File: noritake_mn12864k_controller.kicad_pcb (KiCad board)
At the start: 4 copper layers, 120 parts, among them J1 Conn_01x11, J2 USB_C_Receptacle_USB2.0, J3 TagConnect_TC2030_SWD, Q1 AO3400A, Q10 2N7002, Q11 LBSS84LT1G, Q12 2N7002, Q2 AO3400A, Q3 S9015, Q4 AO3401A, Q5 AO3401A, Q6 S9015, Q7 2N7002, Q8 LBSS84LT1G, Q9 2N7002, T1 Wuerth 760390013, T2 Wuerth 760390013, T3 Wuerth 760390013, U1 SN74AVC8T245PW, U10 XL6007E1, U2 74HC14, U3 CD4051B, U4 MN12864K, U5 STM32F730R8T6, U6 NE555D, U7 74HC08, U8 SRV05-4, U9 XC6206PxxxMR

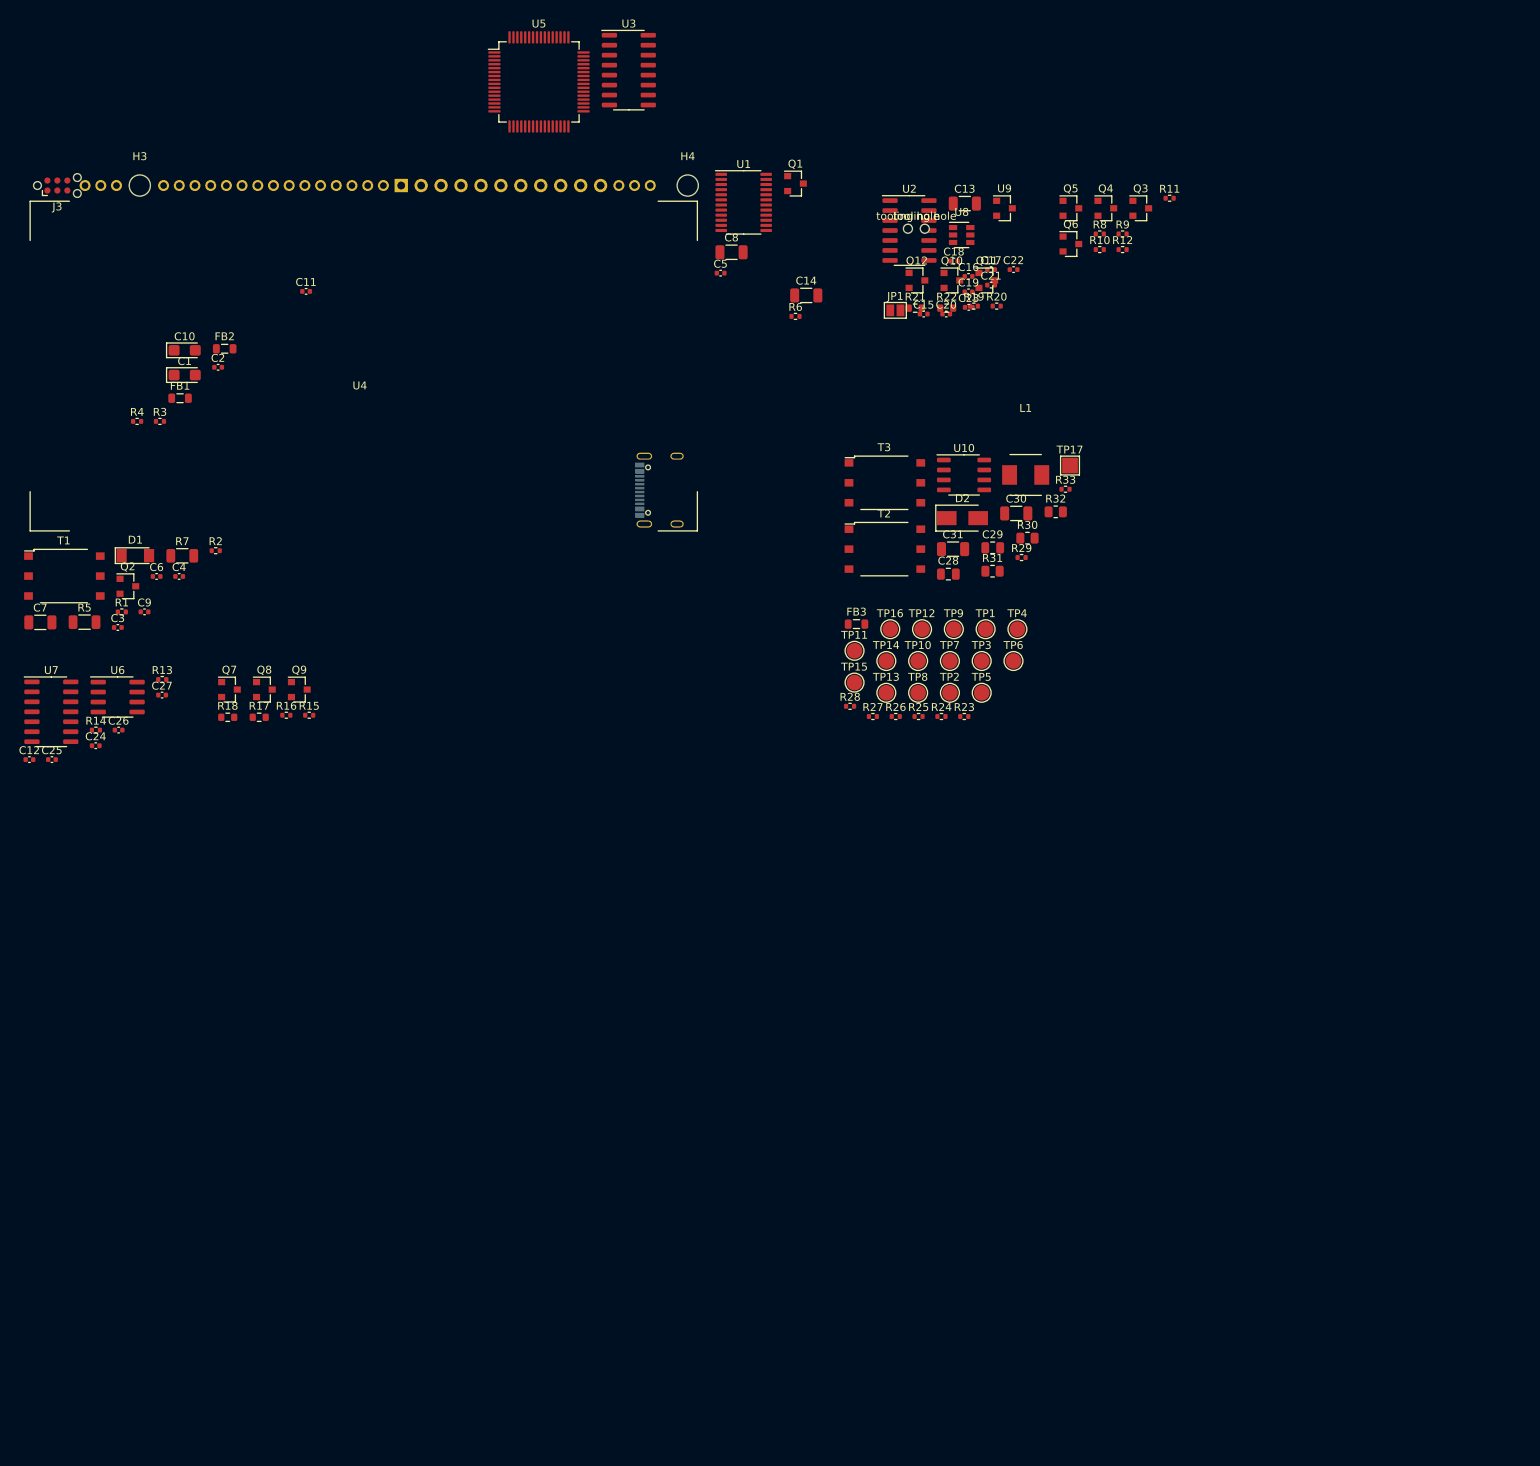
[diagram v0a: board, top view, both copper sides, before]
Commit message: Complete intra section layout
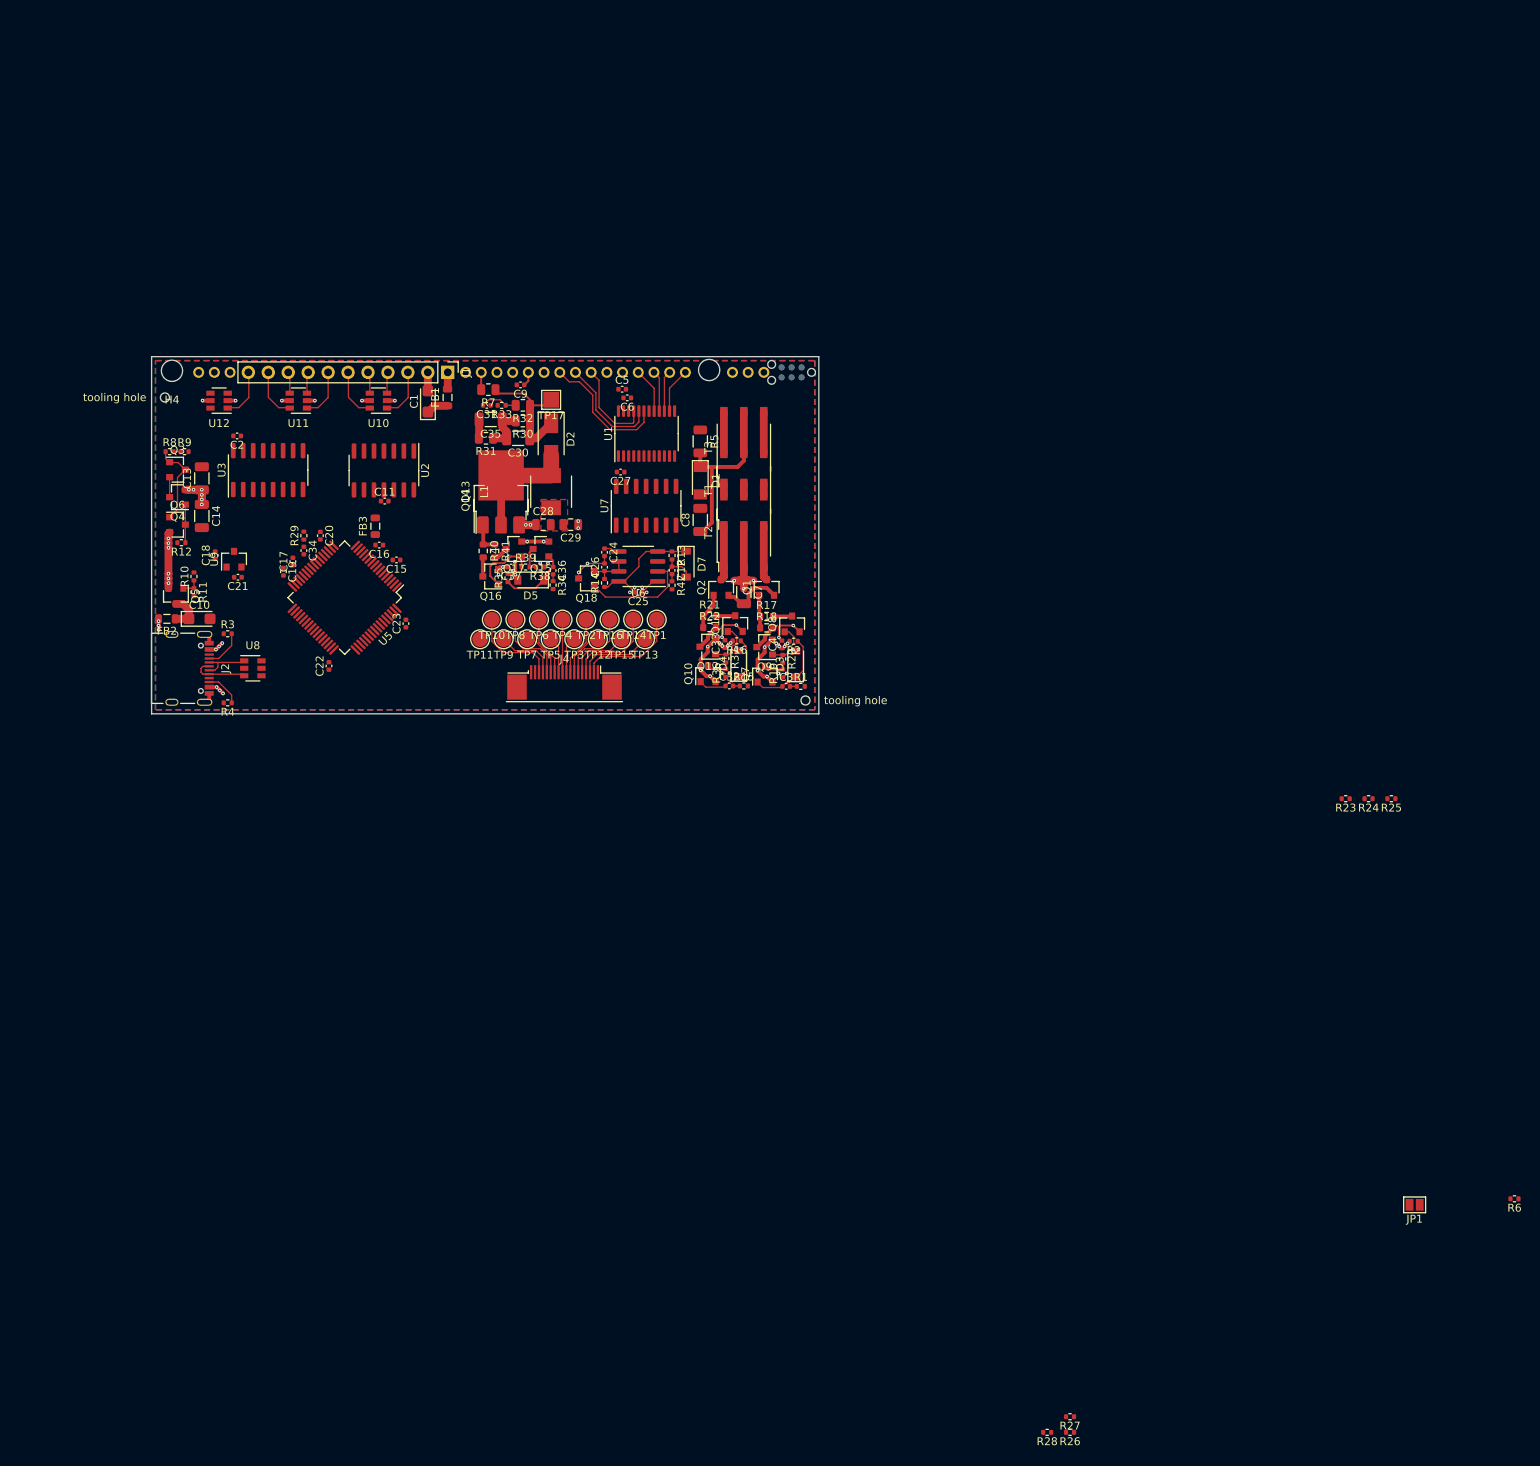
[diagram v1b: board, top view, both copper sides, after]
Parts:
- added C32: 100nF, Capacitor_SMD:C_0402_1005Metric, F.Cu at (173.6, 138.4)
- added C33: 1uF, Capacitor_SMD:C_0402_1005Metric, F.Cu at (173.1, 133.1)
- added C34: 100nF, Capacitor_SMD:C_0402_1005Metric, F.Cu at (119.4, 121.2)
- added C35: 10uF, Capacitor_SMD:C_1206_3216Metric, F.Cu at (143.2, 104.5)
- added C36: 100nF, Capacitor_SMD:C_0402_1005Metric, F.Cu at (151.2, 123.8)
- added C37: 1uF, Capacitor_SMD:C_0402_1005Metric, F.Cu at (145.8, 123.3)
- added D3: B5819W, Diode_SMD:D_SOD-123, F.Cu at (182.1, 135.7)
- added D4: B5819W, Diode_SMD:D_SOD-123, F.Cu at (174.8, 135.6)
- added D5: B5819W, Diode_SMD:D_SOD-123, F.Cu at (148.3, 125.0)
- added D7: B5819W, Diode_SMD:D_SOD-123, F.Cu at (168.1, 122.9)
- added J4: Conn_01x18, Connector_FFC:MINTRON-LW05202-18, F.Cu at (152.6, 135.8)
- added Q13: TO-252, Package_TO_SOT_SMD:TO-252-3_TabPin2, F.Cu at (144.5, 113.7)
- added Q14: CJT04N15, Package_TO_SOT_SMD:SOT-223-3_TabPin2, F.Cu at (144.5, 114.8)
- added Q15: 2N7002, Package_TO_SOT_SMD:SOT-23, F.Cu at (149.6, 121.0)
- added Q16: LBSS84LT1G, Package_TO_SOT_SMD:SOT-23, F.Cu at (143.2, 124.5)
- added Q17: 2N7002, Package_TO_SOT_SMD:SOT-23, F.Cu at (146.2, 121.0)
- added Q18: S9015, Package_TO_SOT_SMD:SOT-23, F.Cu at (155.4, 124.8)
- added R34: 50R, Resistor_SMD:R_0402_1005Metric, F.Cu at (151.2, 125.6)
- added R35: 100kR, Resistor_SMD:R_0402_1005Metric, F.Cu at (145.4, 124.7)
- added R36: 470R, Resistor_SMD:R_0402_1005Metric, F.Cu at (173.2, 136.8)
- added R37: 50R, Resistor_SMD:R_0402_1005Metric, F.Cu at (173.2, 134.9)
- added R38: 470R, Resistor_SMD:R_0402_1005Metric, F.Cu at (149.5, 123.3)
- added R39: 50R, Resistor_SMD:R_0402_1005Metric, F.Cu at (147.7, 123.3)
- added R40: 33R, Resistor_SMD:R_0603_1608Metric, F.Cu at (142.2, 121.2)
- added R41: 33R, Resistor_SMD:R_0603_1608Metric, F.Cu at (143.7, 121.2)
- added R42: 50R, Resistor_SMD:R_0402_1005Metric, F.Cu at (166.3, 125.6)
- added U11: SRV05-4, Package_TO_SOT_SMD:SOT-23-6, F.Cu at (118.7, 102.1)
- added U12: SRV05-4, Package_TO_SOT_SMD:SOT-23-6, F.Cu at (108.6, 102.1)
- C12: value 100nF -> 1nF
- C30: value 4.7uF -> 10uF
- C31: value 4.7uF -> 100nF; footprint Capacitor_SMD:C_1206_3216Metric -> Capacitor_SMD:C_0402_1005Metric
- C4: value 100nF -> 1uF
- H3, J3, U4: moved to B.Cu
- J1, J2: moved to F.Cu
- R1: value 49.9R -> 50R
- R13: value 100kR -> 1MR
- R15: value 100kR -> 50R
- R16: value 1kR -> 100kR
- R19: value 100kR -> 470R
- R2: value 49.9R -> 100kR
- R20: value 1kR -> 50R
- R29: value 100kR -> 5.1kR
- R32: value 36kR -> 100kR
- R33: value 1kR -> 3.3kR
- R7: footprint Resistor_SMD:R_1206_3216Metric -> Resistor_SMD:R_0805_2012Metric
- U10: value XL6007E1 -> SRV05-4; footprint Package_SO:SO-8_3.9x4.9mm_P1.27mm -> Package_TO_SOT_SMD:SOT-23-6
- moved R6 145.0 mm to (273.6, 203.8), turned to 180 degrees
- moved R11 134.0 mm to (105.4, 126.5), turned to 270 degrees
- moved JP1 131.8 mm to (260.9, 204.6), turned to 180 degrees
- moved Q3 127.1 mm to (103.3, 110.9)
- moved R12 125.6 mm to (103.8, 120.2), turned to 180 degrees
- moved Q5 124.3 mm to (103.1, 127.0), turned to 270 degrees
- moved Q4 123.9 mm to (103.3, 114.4), turned to 180 degrees
- moved R9 122.7 mm to (104.2, 108.6)
- moved R10 122.7 mm to (105.4, 124.5), turned to 90 degrees
- moved R8 121.7 mm to (102.3, 108.6)
- moved Q6 119.3 mm to (103.3, 117.9)
- moved U9 107.8 mm to (110.5, 122.3), turned to 90 degrees
- moved U8 105.8 mm to (112.9, 136.2)
- moved C13 103.3 mm to (106.4, 112.0), turned to 90 degrees
- moved C21 102.9 mm to (111.0, 124.6), turned to 180 degrees
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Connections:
- net Net-(J3-Pad2) renamed /SWDIO
- net Net-(J3-Pad4) renamed /SWCLK
- C12 pad 2: /VFD/VFD_GSOUT -> Net-(C12-Pad2)
- C28 pad 1: +5V -> GND
- C28 pad 2: GND -> +5V
- C29 pad 1: +5V -> GND
- C29 pad 2: GND -> +5V
- C3 pad 1: /VFD/G1 -> Net-(C3-Pad1)
- C31 pad 1: Net-(C30-Pad2) -> GND
- C31 pad 2: GND -> /VFD/STEPUP_FB
- C4 pad 1: /VFD/G2 -> GND
- C4 pad 2: Net-(C4-Pad2) -> +5V
- Q10 pad 1: /VFD/G2 -> Net-(C32-Pad1)
- Q11 pad 1: Net-(Q10-Pad3) -> Net-(Q11-Pad1)
- Q12 pad 1: Net-(Q10-Pad3) -> Net-(Q11-Pad1)
- Q7 pad 1: /VFD/G1 -> Net-(C3-Pad1)
- Q8 pad 1: Net-(Q7-Pad3) -> Net-(Q8-Pad1)
- Q9 pad 1: Net-(Q7-Pad3) -> Net-(Q8-Pad1)
- R1 pad 1: /VFD_HTR_G1 -> Net-(C3-Pad2)
- R1 pad 2: Net-(C3-Pad2) -> /VFD_HTR_G1
- R15 pad 1: /VFD/G1 -> Net-(C32-Pad2)
- R15 pad 2: GND -> /VFD_HTR_G2
- R16 pad 1: +5V -> Net-(C32-Pad1)
- R16 pad 2: Net-(Q7-Pad3) -> GND
- R19 pad 1: /VFD/G2 -> +5V
- R19 pad 2: GND -> Net-(Q7-Pad3)
- R2 pad 1: /VFD_HTR_G2 -> Net-(C3-Pad1)
- R2 pad 2: Net-(C4-Pad2) -> GND
- R20 pad 1: +5V -> Net-(Q8-Pad1)
- R20 pad 2: Net-(Q10-Pad3) -> Net-(Q7-Pad3)
- R25 pad 1: /IFSEL -> +3V3
- R25 pad 2: +3V3 -> /IFSEL
- R26 pad 1: /~SHDWN -> +3V3
- R26 pad 2: +3V3 -> /4WIRE
- R27 pad 1: /4WIRE -> +3V3
- R27 pad 2: +3V3 -> /CPOL
- R28 pad 1: /CPOL -> +3V3
- R28 pad 2: +3V3 -> /~SHDWN
- R29 pad 1: GND -> /VFD_HV_FB
- R29 pad 2: /VFD_HV_EN -> /VFD/STEPUP_FB
- R32 pad 2: Net-(R32-Pad2) -> /VFD/STEPUP_FB
- R33 pad 1: Net-(R32-Pad2) -> /VFD/STEPUP_FB
- U10 pad 1: /VFD_HV_EN -> /CPOL
- U10 pad 2: +5V -> GND
- U10 pad 3: Net-(R32-Pad2) -> /4WIRE
- U10 pad 4: (no net) -> /~RST
- U10 pad 5: Net-(D2-Pad2) -> +5V
- U10 pad 6: Net-(D2-Pad2) -> /~DC
- U2 pad 9: Net-(U2-Pad9) -> GND
- U4 pad 1: Net-(U4-Pad1) -> Net-(T1-Pad4)
- U4 pad 2: Net-(U4-Pad1) -> Net-(T1-Pad4)
- U4 pad 3: Net-(U4-Pad1) -> Net-(T1-Pad4)
- U4 pad 35: Net-(U4-Pad35) -> Net-(T1-Pad6)
- U4 pad 36: Net-(U4-Pad35) -> Net-(T1-Pad6)
- U4 pad 37: Net-(U4-Pad35) -> Net-(T1-Pad6)
- U5 pad 10: /DBG08 -> /DBG10
- U5 pad 11: /DBG09 -> /DBG11
- U5 pad 2: Net-(U5-Pad2) -> /DBG14
- U5 pad 20: /~CS -> /VFD_BLK
- U5 pad 21: /SCK_GATED -> /VFD_GSBLK
- U5 pad 22: /VFD_GLAT -> /VFD_LAT
- U5 pad 23: /MOSI -> /VFD_GLAT
- U5 pad 24: /DBG10 -> /DBG12
- U5 pad 25: /VFD_BLK -> /VFD_HV_FB
- U5 pad 26: /VFD_GSBLK -> /DBG01
- U5 pad 27: /DBG05 -> /DBG07
- U5 pad 28: /DBG01 -> /~SHDWN
- U5 pad 29: /DBG02 -> /DBG04
- U5 pad 3: Net-(U5-Pad3) -> /DBG15
- U5 pad 33: /DBG03 -> /DBG05
- U5 pad 35: /DBG04 -> /DBG06
- U5 pad 37: /DBG11 -> /VFD_HV_G
- U5 pad 38: /DBG12 -> Net-(U5-Pad38)
- U5 pad 39: /DBG13 -> Net-(U5-Pad39)
- U5 pad 40: /DBG14 -> Net-(U5-Pad40)
- U5 pad 42: /VFD_LAT -> /DBG00
- U5 pad 50: /VFD_HV_EN -> /~CS
- U5 pad 51: /DBG15 -> /VFD_GCLK
- U5 pad 52: Net-(U5-Pad52) -> /DBG13
- U5 pad 53: Net-(U5-Pad53) -> /VFD_GSIN
- U5 pad 55: /VFD_GCLK -> /SCK_GATED
- U5 pad 56: /IFSEL -> /DBG02
- U5 pad 57: /VFD_GSIN -> /MOSI
- U5 pad 58: /~SHDWN -> /DBG03
- U5 pad 62: /DBG00 -> /IFSEL
- U5 pad 8: /DBG06 -> /DBG08
- U5 pad 9: /DBG07 -> /DBG09
- U6 pad 3: Net-(U2-Pad9) -> Net-(U6-Pad3)
- U7 pad 1: Net-(U2-Pad8) -> Net-(U6-Pad3)
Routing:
- net +5V: track 0.00 -> 58.6 mm, vias 0 -> 32
- net GND: track 0.00 -> 56.2 mm, vias 0 -> 34
- net Net-(FB2-Pad2): track 0.00 -> 24.8 mm, vias 0 -> 9
- net Net-(C8-Pad1): track 0.00 -> 23.0 mm
- net Net-(C12-Pad1): track 0.00 -> 18.2 mm
- net Net-(U1-Pad19): track 0.00 -> 16.9 mm
- net +48V: track 0.00 -> 15.8 mm
- net Net-(D2-Pad2): track 0.00 -> 15.2 mm
- net Net-(U1-Pad20): track 0.00 -> 13.8 mm
- net /DBG00: track 0.00 -> 13.6 mm
- net /DBG14: track 0.00 -> 11.9 mm
- net /DBG02: track 0.00 -> 11.9 mm
- net Net-(U1-Pad21): track 0.00 -> 11.7 mm
- net Net-(C3-Pad1): track 0.00 -> 10.9 mm
- net Net-(C32-Pad1): track 0.00 -> 10.9 mm
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- added copper zone on F.Cu, net +5V
- added copper zone on Power, net +5V
- added copper zone on B.Cu, net GND
- added copper zone on F.Cu, net GND
- added copper zone on GND, net GND
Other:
- board outline added: 85 x 45.5 mm
- net class HV added: clearance 0.5, trace_width 0.09, via_dia 0.45, via_drill 0.2

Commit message: Layout all nets
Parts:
- moved R6 155.4 mm to (133.3, 136.8), turned to 270 degrees
- moved JP1 145.0 mm to (134.0, 134.4), turned to 0 degrees
- moved R28 144.9 mm to (118.7, 124.5), turned to 315 degrees
- moved R24 134.0 mm to (125.0, 120.8), turned to 225 degrees
- moved R27 129.1 mm to (134.2, 132.6)
- moved R26 128.5 mm to (132.3, 136.8), turned to 90 degrees
- moved R25 125.6 mm to (134.2, 131.6)
- moved R23 125.2 mm to (127.9, 137.0), turned to 0 degrees
- moved D7 13.9 mm to (154.3, 124.3), turned to 90 degrees
- moved Q18 11.8 mm to (167.0, 122.5), turned to 0 degrees
- moved R42 11.0 mm to (156.1, 121.6), turned to 90 degrees
- moved R13 10.8 mm to (156.1, 125.4), turned to 90 degrees
- moved C12 10.2 mm to (156.1, 123.5), turned to 90 degrees
- moved C18 8.80 mm to (115.1, 116.5)
- moved U9 8.78 mm to (117.5, 117.0)
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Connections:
- U2 pad 1: /~CS -> /CPOL
- U2 pad 5: /CPOL -> /~CS
- U3 pad 11: Net-(U2-Pad2) -> Net-(U2-Pad6)
- U3 pad 9: Net-(U2-Pad6) -> Net-(U2-Pad2)
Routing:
- net +3V3: track 0.00 -> 102.3 mm, vias 0 -> 18
- net /~MCU_RST: track 0.00 -> 98.4 mm, vias 0 -> 3
- net /SWDIO: track 0.00 -> 94.3 mm, vias 0 -> 3
- net /SWCLK: track 0.00 -> 91.0 mm, vias 0 -> 3
- net /VFD_SIN: track 0.00 -> 82.6 mm, vias 0 -> 6
- net /VFD_CLK: track 0.00 -> 80.1 mm, vias 0 -> 6
- net Net-(T1-Pad6): track 5.39 -> 83.7 mm, vias 0 -> 4
- net /VFD_HTR_G1: track 0.00 -> 68.1 mm, vias 0 -> 2
- net /VFD_GCLK: track 0.00 -> 65.3 mm, vias 0 -> 4
- net /VFD_GSIN: track 0.00 -> 64.0 mm, vias 0 -> 4
- net /VFD_HTR_G2: track 0.00 -> 62.7 mm, vias 0 -> 2
- net /DBG01: track 10.1 -> 72.4 mm, vias 0 -> 2
- net /VFD_GLAT: track 0.00 -> 60.2 mm, vias 0 -> 4
- net /VFD_LAT: track 0.00 -> 59.4 mm, vias 0 -> 4
- net /MOSI: track 2.73 -> 61.6 mm, vias 0 -> 4
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- added copper zone on Power, net +3V3
